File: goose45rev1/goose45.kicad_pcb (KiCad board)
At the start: 2 copper layers, 247 x 74.8 mm, 141 parts, among them J1 USB_C_Receptacle_USB2.0, J2 SPI, J3 Conn_01x05_Male, J4 Debugger, J5 USART, SW1 Conn_01x02_Female, SW10 SW_Push, SW11 SW_Push, SW12 SW_Push, SW13 SW_Push, SW14 SW_Push, SW15 SW_Push, SW16 SW_Push, SW17 SW_Push, SW18 SW_Push, SW19 SW_Push, SW2 SW_Push, SW20 SW_Push, SW21 SW_Push, SW22 SW_Push, SW23 SW_Push, SW24 SW_Push, SW25 SW_Push, SW26 SW_Push, SW27 SW_Push, SW28 SW_Push, SW29 SW_Push, SW3 SW_Push, SW30 SW_Push, SW31 SW_Push, SW32 SW_Push, SW33 SW_Push, SW34 SW_Push, SW35 SW_Push, SW36 SW_Push, SW37 SW_Push, SW38 SW_Push, SW39 SW_Push, SW4 SW_Push, SW40 SW_Push, SW41 SW_Push, SW42 SW_Push, SW43 SW_Push, SW44 SW_Push, SW45 SW_Push, SW46 SW_Push, SW48 SW_Push, SW5 SW_Push, SW6 SW_Push, SW7 SW_Push, SW8 SW_Push, SW9 SW_Push, U1 STM32F103CBTx, U2 USBLC6-2SC6, U3 TLV75533PDBV, X1 Crystal_GND24

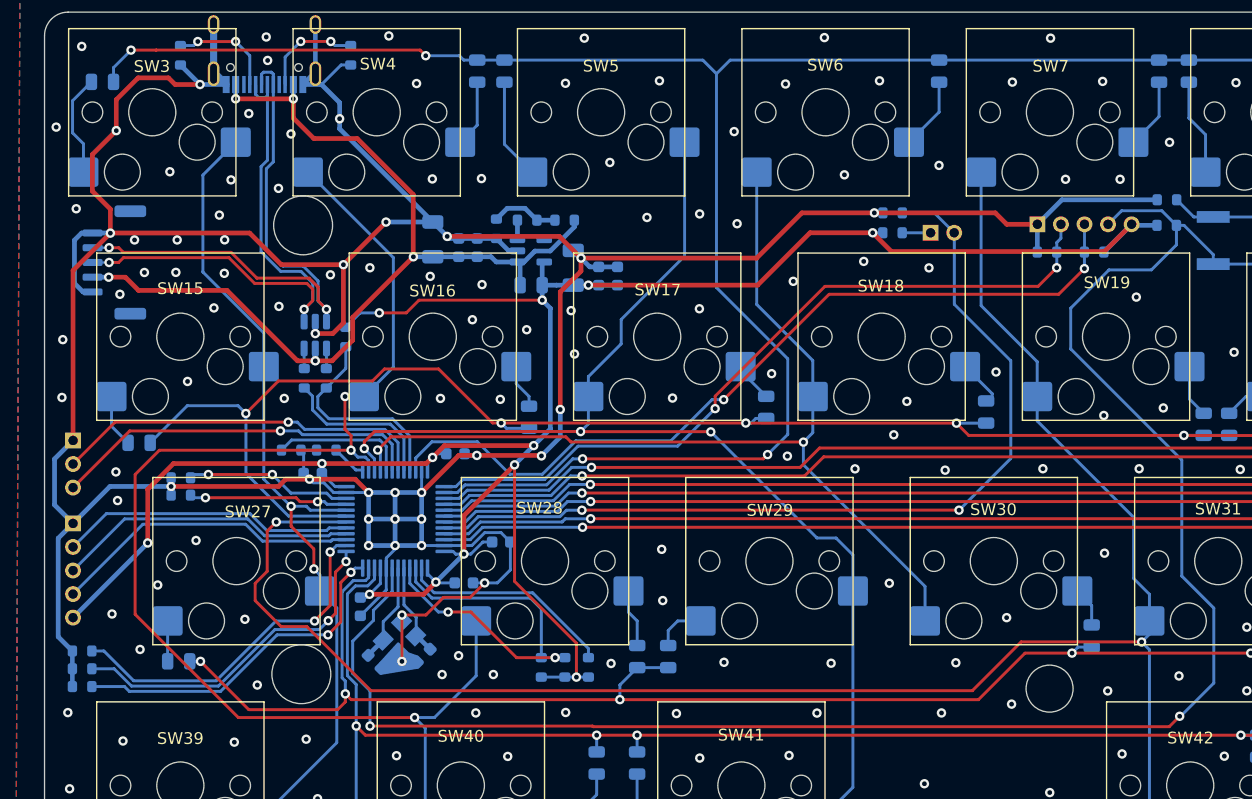
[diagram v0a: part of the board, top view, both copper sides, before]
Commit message: remove the usb conn on rev1
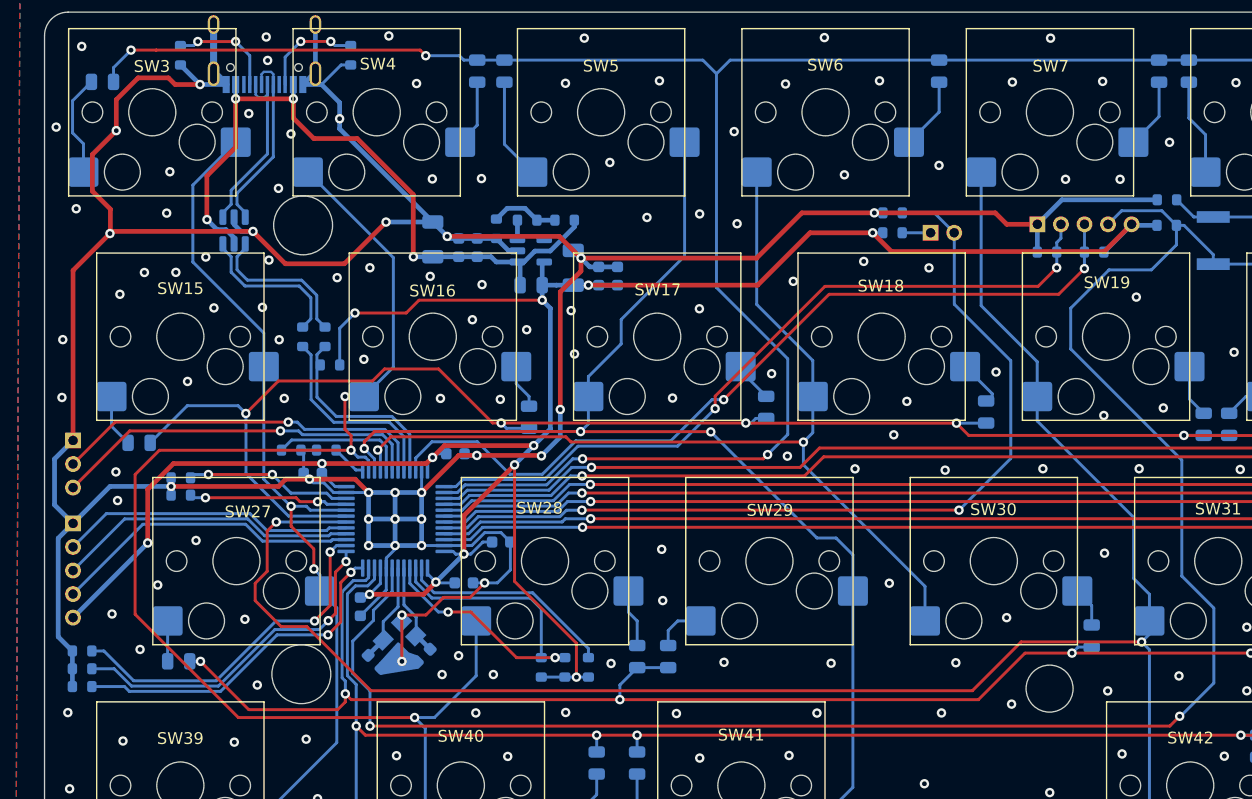
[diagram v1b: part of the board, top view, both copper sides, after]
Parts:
- removed the J3 at (32.2, 79.7)
- moved U2 11.2 mm to (42.3, 77.0)
- moved R15 3.52 mm to (48.1, 86.0)
- moved R18 3.52 mm to (50.0, 86.0)
- moved R19 2.72 mm to (50.5, 88.4), turned to 0 degrees
- renumbered J4 to J3
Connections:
- net Net-(R15-Pad1) renamed /Interface/USBTVSD-
- net Net-(R18-Pad1) renamed /Interface/USBTVSD+
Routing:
- net /Interface/USBD+: track 49.1 -> 15.7 mm, vias 2 -> 0
- net /Interface/USBD-: track 47.7 -> 15.4 mm, vias 2 -> 0
- net VIN: track 80.9 -> 59.6 mm, vias 5 -> 4
- net GND: track 363.0 -> 348.0 mm, vias 306 -> 304
- net /Interface/USBTVSD-: track 1.71 -> 13.1 mm
- net /Interface/USBTVSD+: track 1.71 -> 13.1 mm
- net +3.3V: track 206.7 -> 210.4 mm
- net USB_D-: track 13.6 -> 16.8 mm
- net USB_D+: track 17.8 -> 16.8 mm
- net col1: track 70.4 -> 71.1 mm

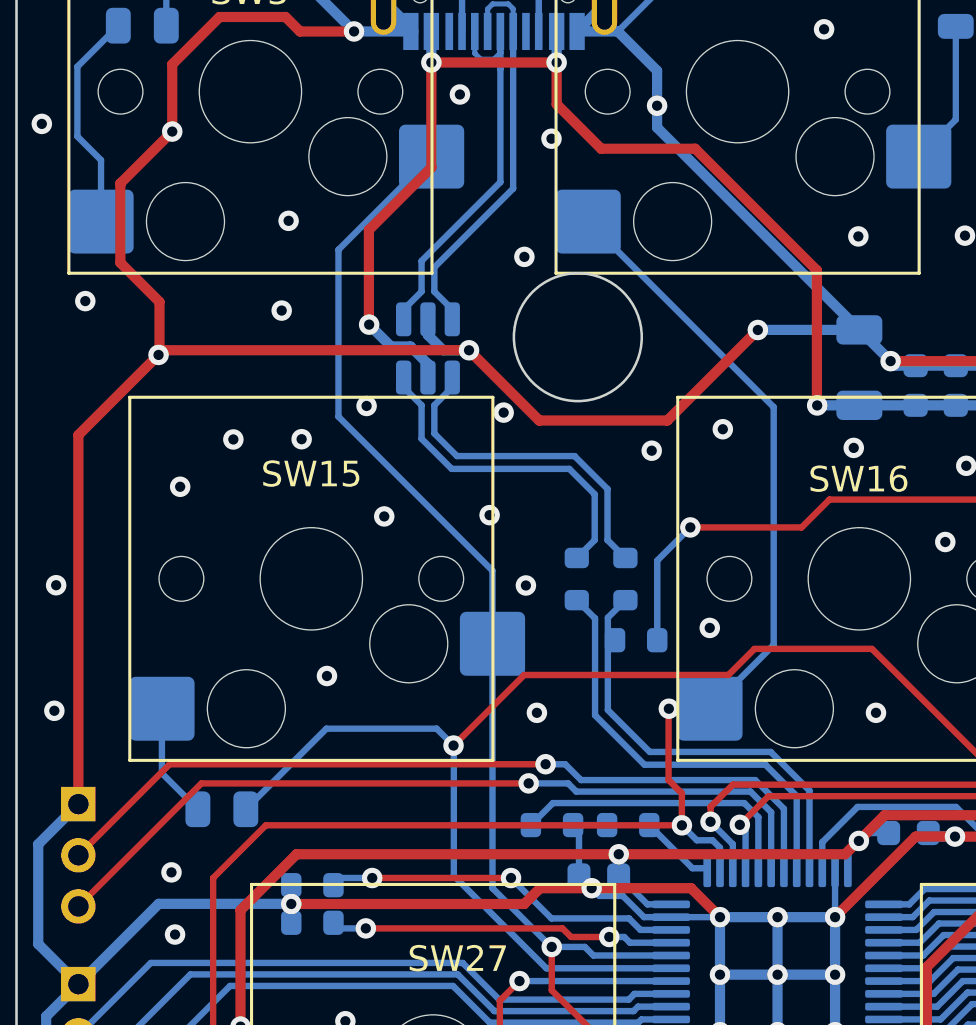
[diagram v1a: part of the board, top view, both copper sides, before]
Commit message: update usb layout and add connector
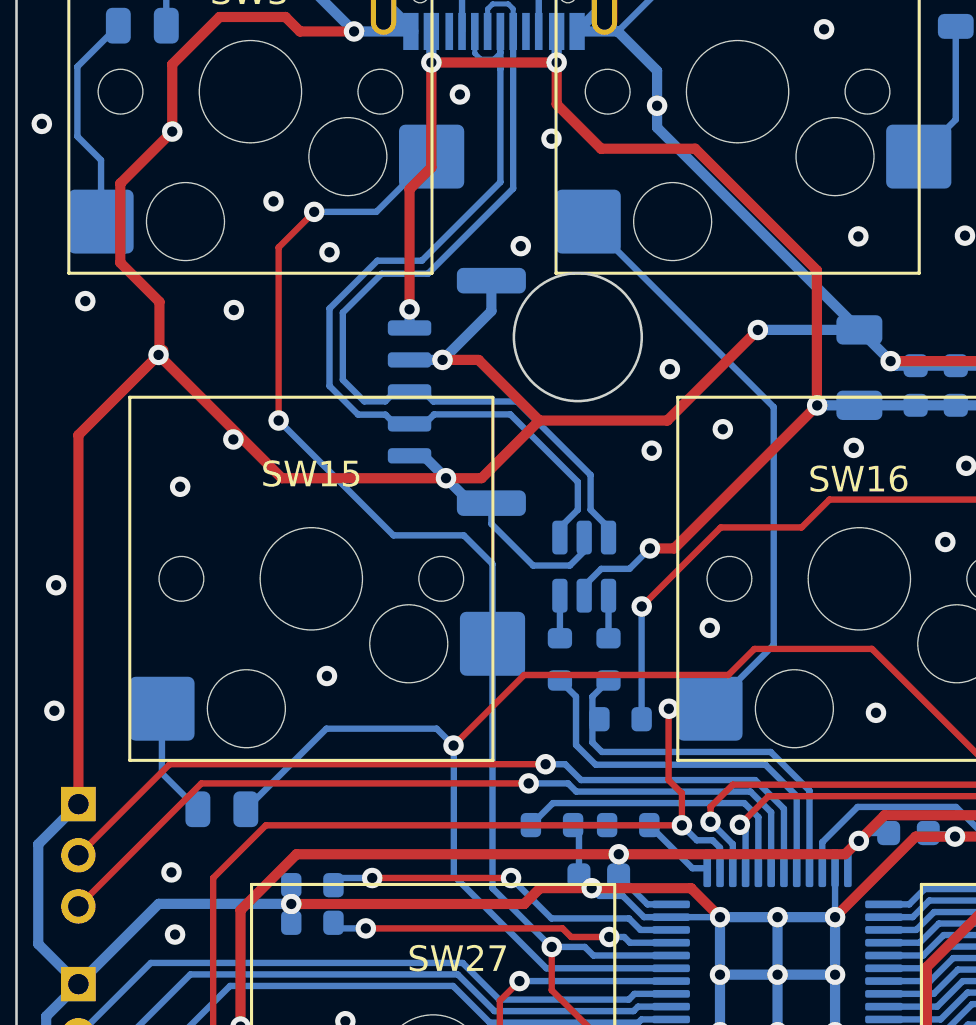
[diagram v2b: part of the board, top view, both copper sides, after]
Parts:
- added J4: USB connector, Connector_Molex:Molex_CLIK-Mate_502386-0570_1x05-1MP_P1.25mm_Horizontal, B.Cu at (43.5, 78.7)
- moved U2 10.5 mm to (48.4, 85.6)
- moved R15 3.21 mm to (47.5, 89.2)
- moved R18 3.21 mm to (49.4, 89.2)
- moved R19 3.15 mm to (49.9, 91.5)
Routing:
- net GND: track 348.0 -> 367.3 mm, vias 304 -> 300
- net /Interface/USBD+: track 15.7 -> 34.6 mm
- net /Interface/USBD-: track 15.4 -> 34.2 mm
- net /Interface/USBTVSD-: track 13.1 -> 1.66 mm
- net /Interface/USBTVSD+: track 13.1 -> 1.66 mm
- net VIN: track 59.6 -> 68.0 mm, vias 4 -> 5
- net col1: track 71.1 -> 76.1 mm, vias 2 -> 4
- net +3.3V: track 210.4 -> 213.0 mm
- net USB_D+: track 16.8 -> 15.0 mm
- net USB_D-: track 16.8 -> 15.1 mm

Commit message: change Diode pcb pad and modify usb connector location
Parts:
- D10, D11, D12, D13, D14, D15, D16, D17, D18, D19, D2, D20, D21, D22, D23, D24, D25, D26, D27, D28, D29, D3, D30, D31, D32, D33, D34, D35, D36, D37, D38, D39, D4, D40, D41, D42, D43, D44, D45, D46, D48, D5, D6, D7, D8, D9: footprint Diode_SMD:D_0805_2012Metric -> Diode_SMD:D_SOD-323
- moved D40 1.88 mm to (73.0, 124.1)
- moved D41 1.88 mm to (76.6, 124.1)
- moved R17 1.32 mm to (50.9, 61.8)
- moved J1 0.65 mm to (44.3, 60.4)
- moved R16 0.50 mm to (37.5, 61.7)
- moved D26 0.11 mm to (262.9, 94.5)
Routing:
- net row4: track 292.9 -> 305.8 mm, vias 8 -> 7
- net RESET: track 155.8 -> 143.4 mm
- net col5: track 158.1 -> 163.9 mm
- net row3: track 259.9 -> 264.6 mm
- net Net-(D41-Pad2): track 7.30 -> 5.29 mm
- net Net-(D40-Pad2): track 6.93 -> 5.00 mm
- net col1: track 76.1 -> 75.0 mm
- net Net-(J1-PadB5): track 8.59 -> 7.60 mm
- net /Interface/CC: track 8.97 -> 8.05 mm
- net /Interface/USBD-: track 34.2 -> 34.9 mm
- net col2: track 114.3 -> 113.7 mm
- net GND: track 367.3 -> 367.5 mm, vias 300 -> 310
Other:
- outline, holes or cut-outs redrawn
- board text added: "Make your ideas come true."
- board text removed: "Build your keyboard and enjoy that time."
